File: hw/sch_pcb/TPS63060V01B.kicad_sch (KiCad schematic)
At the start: 40 parts, among them P1 1,1A, X1 SROUB3M, X2 SROUB3M, X3 SROUB3M, X4 SROUB3M, X5 TPS63060, X9 APX809

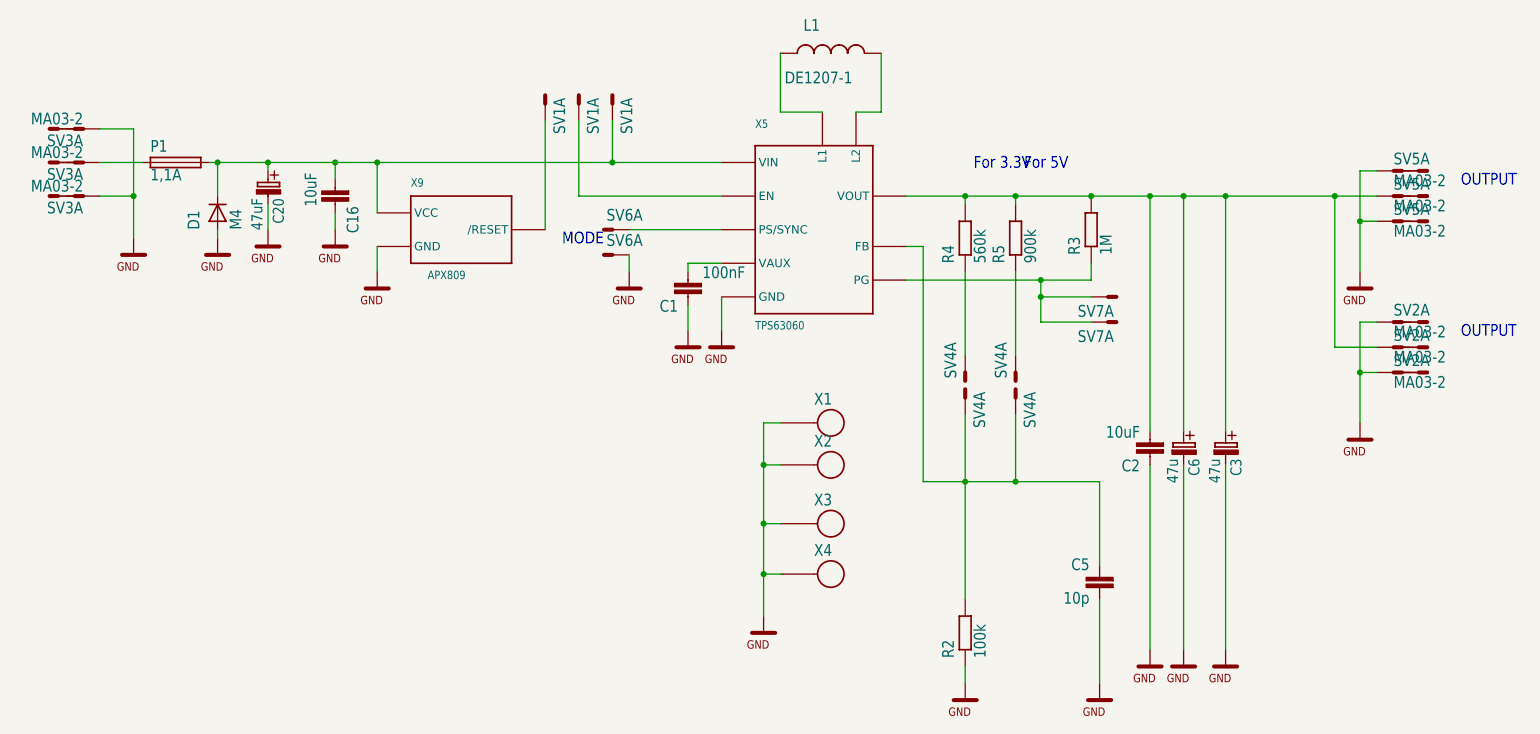
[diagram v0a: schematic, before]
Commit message: urpava shema a pouzder kvuli prechodu z eagle
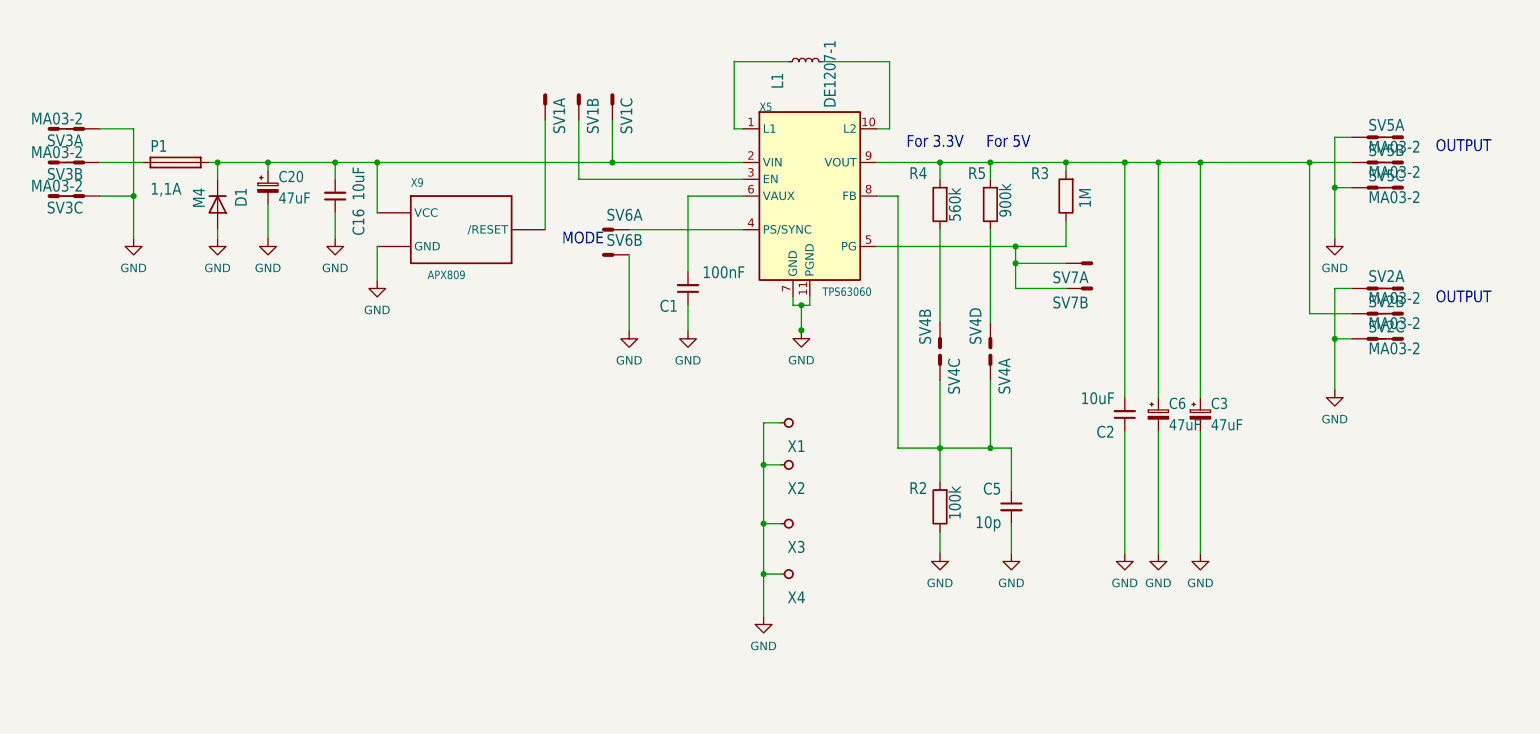
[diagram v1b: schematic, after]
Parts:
- C1, C16, C2, C5: footprint untitled:C0805 -> Capacitor_SMD:C_0805_2012Metric; symbol untitled-eagle-import:C0805 -> Device:C_Small
- C20: footprint untitled:C -> Mlab_C:TantalC_SizeC_Reflow; symbol untitled-eagle-import:C -> Device:C_Polarized_Small
- C3, C6: value 47u -> 47uF; footprint untitled:C -> Mlab_C:TantalC_SizeC_Reflow; symbol untitled-eagle-import:C -> Device:C_Polarized_Small
- D1: footprint untitled:SMA -> Diode_SMD:D_SMA; symbol untitled-eagle-import:D-OB.SMA -> Device:D
- L1: footprint untitled:DE1205-10 -> Mlab_L:DE1205-10; symbol untitled-eagle-import:DE1205-10 -> Device:L_Small
- P1: footprint untitled:1812 -> Mlab_F:1812
- R2, R3, R4, R5: footprint untitled:0805 -> Resistor_SMD:R_0805_2012Metric; symbol untitled-eagle-import:R0805 -> Device:R
- X1, X2, X3, X4: footprint untitled:SROUB3M -> Mlab_Mechanical:MountingHole_3mm; symbol untitled-eagle-import:SROUB3M -> MLAB_MECHANICAL:HOLE
- X5: footprint untitled:SON10 -> Package_SON:Texas_S-PWSON-N10_ThermalVias; symbol untitled-eagle-import:TPS63060 -> Regulator_Switching:TPS63060
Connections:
- net GND: now also C20.2, C3.2, C6.2, D1.2 (A), SV2.5 (K), SV2.6 (K), SV3.5 (K), SV3.6 (K), SV5.5 (K), SV5.6 (K), SV6.2 (P$1), X1.1, X2.1, X3.1, X4.1; no longer C20.- (C_EL-), C3.- (C_EL-), C6.- (C_EL-), D1.A, SV2.1 (K), SV2.2 (K), SV3.1 (K), SV3.2 (K), SV5.1 (K), SV5.2 (K), SV6.1 (P$1), X1.P$1, X2.P$1, X3.P$1, X4.P$1, X5.12 (GND), X5.13 (GND), X5.14 (GND), X5.15 (GND), X5.16 (GND), X5.17 (GND), X5.18 (GND), X5.19 (GND), X5.21 (GND), X5.P$1 (GND), X5.P$2 (GND), X5.P$3 (GND), X5.P$4 (GND), X5.P$5 (GND)
- net at C5.1, R2.2, SV4.1 (P$1)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: now also SV4.3 (P$1); no longer SV4.1 (P$1)
- net at R4.1: now also SV4.2 (P$1); no longer SV4.1 (P$1)
- net at X5.1 (L1): now also L1.1; no longer L1.P$1 (1)
- net at X5.10 (L2): now also L1.2; no longer L1.P$2 (2)
- net at R3.1, SV7.1 (P$1), X5.5 (PG): now also SV7.2 (P$1); no longer SV7.1 (P$1)
- net at C16.2, P1.2, X5.2 (VIN)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: now also C20.1, D1.1 (K), SV1.3 (P$1); no longer C20.+ (C_EL+), D1.K (C), SV1.1 (P$1)
- net at R5.1: now also SV4.4 (P$1); no longer SV4.1 (P$1)
- net at X5.3 (EN): now also SV1.2 (P$1); no longer SV1.1 (P$1)
- new net: C2.2, C3.1, C6.1, R3.2, R4.2, R5.2, SV2.3 (K), SV2.4 (K), SV5.3 (K), SV5.4 (K), X5.9 (VOUT)
- new net: P1.1, SV3.3 (K), SV3.4 (K)
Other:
- moved on the sheet: SV2A, SV2B, SV2C, SV4A, SV4B, SV4C, SV4D, SV5A, SV5B, SV5C, SV7A, SV7B
